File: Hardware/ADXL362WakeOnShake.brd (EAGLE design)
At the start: 43.2 x 24.1 mm, 23 parts, among them J1 PROG_HDR, U1 ADXL362, U3 ADP160-3.3

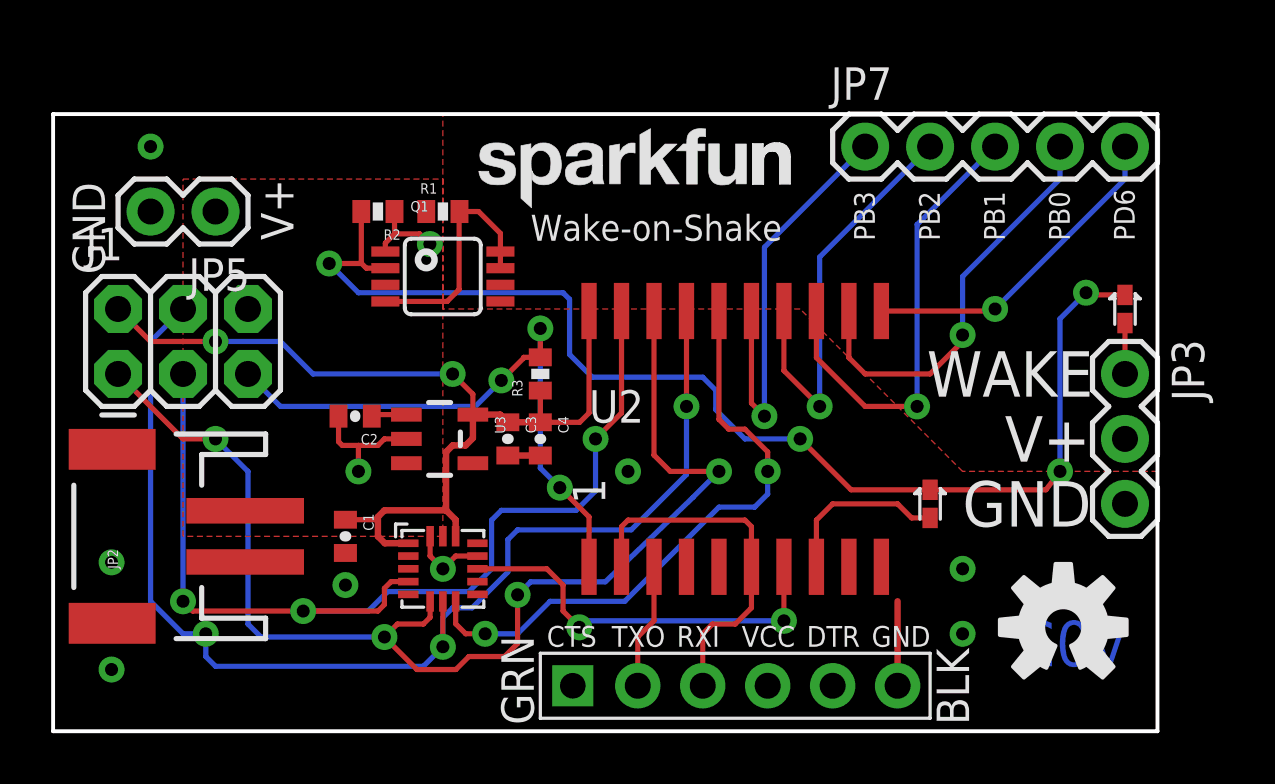
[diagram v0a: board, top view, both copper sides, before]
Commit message: Updating hardware files to v10: - FTDI header silk changed to accurately reflect pin names - moved some traces to avoid silk/via collision - added 10k resistor pull-up on RX line - FTDI header was slightly off grid - added silk on ATTiny package.
Changes to Firmware are purely machine changes to project files.
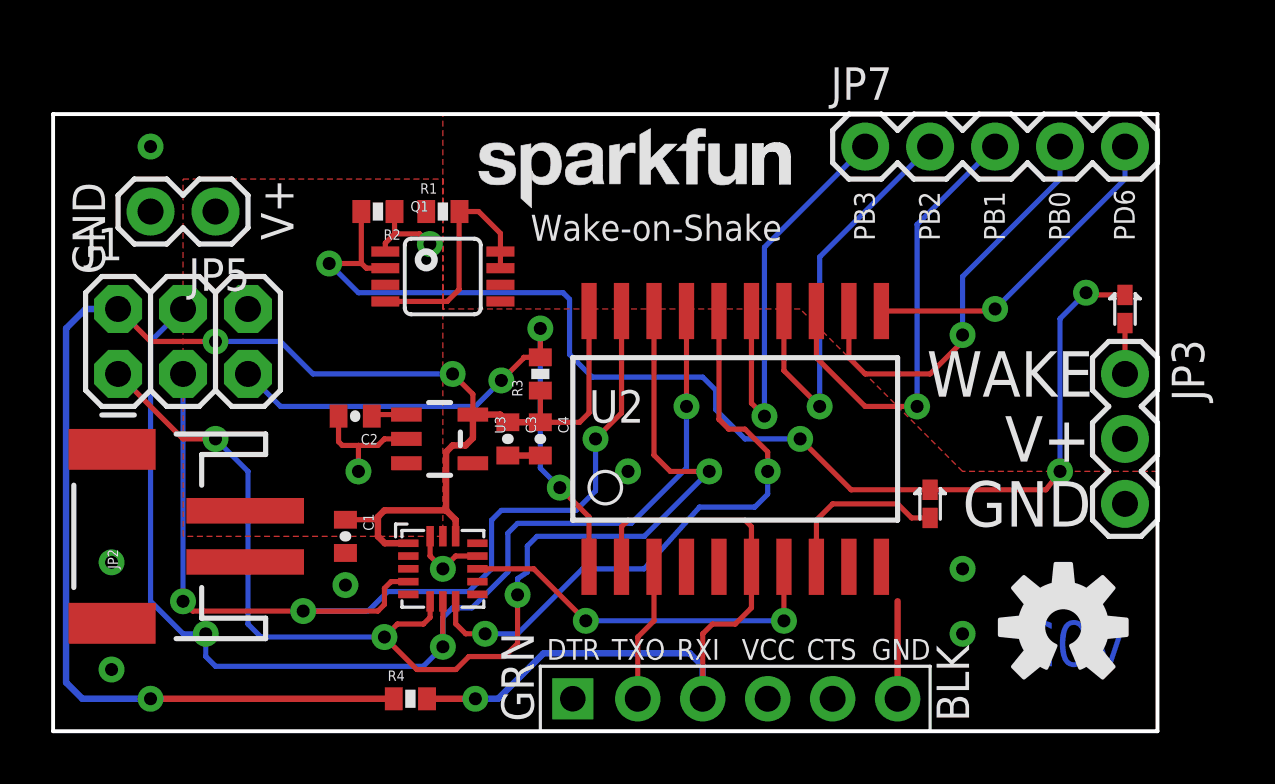
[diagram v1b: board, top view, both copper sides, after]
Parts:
- added R4: 10k, SparkFun-Passives:0402-RES
- moved JP1 0.51 mm to (26.7, 1.27)
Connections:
- net 3.3V: now also R4.1
- net RXI: now also R4.2
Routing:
- net 3.3V: track 38.2 -> 67.5 mm, vias 2 -> 3
- net RXI: track 15.1 -> 28.6 mm, vias 0 -> 1
- net INT1: track 15.7 -> 14.9 mm
- net TXO: track 4.92 -> 5.42 mm
- net GND: track 16.4 -> 16.9 mm
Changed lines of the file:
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@@
 </element>
 <element name="JP3" library="SparkFun-Connectors" package="1X03" value="" x="41.91" y="13.97" rot="R270"/>
-<element name="JP1" library="SparkFun-Connectors" package="FTDI_DEVICE_SIDE" value="FTDI_DEVICE" x="26.67" y="1.778"/>
+<element name="JP1" library="SparkFun-Connectors" package="FTDI_DEVICE_SIDE" value="FTDI_DEVICE" x="26.67" y="1.27"/>
 <element name="D2" library="SparkFun-DiscreteSemi" package="SOD-523" value="RB751" x="34.29" y="8.89" rot="R90">
 <attribute name="PROD_ID" value="DIO-11018" x="34.29" y="8.89" size="1.778" layer="27" font="vector" ratio="15" rot="R90" display="off"/>
@@
 <attribute name="DIST_ID" value="ADP160AUJZ-3.3-R7TR-ND" x="15.113" y="11.43" size="1.778" layer="27" rot="R270" display="off"/>
 <attribute name="DIST" value="Digikey" x="15.113" y="11.43" size="1.778" layer="27" rot="R270" display="off"/>
+<attribute name="PROD_ID" value="VREG-11306" x="15.113" y="11.43" size="1.778" layer="27" rot="R270" display="off"/>
+<attribute name="VALUE" value="ADP160" x="15.113" y="11.43" size="1.778" layer="27" rot="R270" display="off"/>
 </element>
 <element name="R2" library="SparkFun-Passives" package="0402-RES" value="1M" x="12.7" y="20.32" rot="R180">
@@
 <element name="JP6" library="SparkFun-Aesthetics" package="SFE-NEW-WEBLOGO" value="LOGO-SFENEW" x="36.322" y="15.494" rot="MR0"/>
 <element name="JP7" library="SparkFun-Connectors" package="1X05" value="" x="31.75" y="22.86"/>
+<element name="R4" library="SparkFun-Passives" package="0402-RES" value="10k" x="13.97" y="1.27">
+<attribute name="PROD_ID" value="RES-00824" x="13.97" y="1.27" size="1.778" layer="27" font="vector" ratio="15" display="off"/>
+</element>
 </elements>
 <signals>
@@
 <contactref element="JP1" pad="P$6"/>
 <wire x1="32.385" y1="6.43" x2="32.385" y2="5.715" width="0.254" layer="1"/>
-<wire x1="33.02" y1="5.08" x2="33.02" y2="1.778" width="0.254" layer="1"/>
+<wire x1="33.02" y1="5.08" x2="33.02" y2="1.27" width="0.254" layer="1"/>
 <wire x1="17.78" y1="10.78" x2="19.05" y2="10.78" width="0.254" layer="1"/>
 <wire x1="12.99" y1="18.755" x2="12.99" y2="19.086" width="0.2032" layer="1"/>
@@
 <via x="28.575" y="4.318" extent="1-16" drill="0.508"/>
 <wire x1="28.575" y1="4.318" x2="20.828" y2="4.318" width="0.2032" layer="16"/>
-<wire x1="20.828" y1="4.318" x2="20.574" y2="4.064" width="0.2032" layer="16"/>
-<via x="20.574" y="4.064" extent="1-16" drill="0.508"/>
-<wire x1="20.574" y1="4.064" x2="19.939" y2="4.699" width="0.2032" layer="1"/>
-<wire x1="19.939" y1="4.699" x2="19.939" y2="5.715" width="0.2032" layer="1"/>
-<wire x1="19.939" y1="5.715" x2="19.304" y2="6.35" width="0.2032" layer="1"/>
-<wire x1="19.304" y1="6.35" x2="16.59" y2="6.35" width="0.2032" layer="1"/>
+<via x="20.828" y="4.318" extent="1-16" drill="0.508"/>
+<wire x1="20.828" y1="4.318" x2="18.796" y2="6.35" width="0.2032" layer="1"/>
+<wire x1="18.796" y1="6.35" x2="16.59" y2="6.35" width="0.2032" layer="1"/>
 </signal>
 <signal name="3.3V">
@@
 <wire x1="6.35" y1="15.24" x2="3.81" y2="15.24" width="0.2032" layer="1"/>
 <wire x1="3.81" y1="15.24" x2="2.54" y2="16.51" width="0.2032" layer="1"/>
+<contactref element="R4" pad="1"/>
+<wire x1="13.32" y1="1.27" x2="3.81" y2="1.27" width="0.254" layer="1"/>
+<via x="3.81" y="1.27" extent="1-16" drill="0.508"/>
+<wire x1="3.81" y1="1.27" x2="1.143" y2="1.27" width="0.254" layer="16"/>
+<wire x1="1.143" y1="1.27" x2="0.508" y2="1.905" width="0.254" layer="16"/>
+<wire x1="0.508" y1="1.905" x2="0.508" y2="15.748" width="0.254" layer="16"/>
+<wire x1="0.508" y1="15.748" x2="1.27" y2="16.51" width="0.254" layer="16"/>
+<wire x1="1.27" y1="16.51" x2="2.54" y2="16.51" width="0.254" layer="16"/>
 </signal>
 <signal name="SCK">
@@
 <via x="15.24" y="3.302" extent="1-16" drill="0.508"/>
 <wire x1="16.383" y1="4.826" x2="17.78" y2="6.223" width="0.2032" layer="16"/>
-<wire x1="17.78" y1="6.223" x2="17.78" y2="7.493" width="0.2032" layer="16"/>
-<wire x1="17.78" y1="7.493" x2="18.161" y2="7.874" width="0.2032" layer="16"/>
-<wire x1="18.161" y1="7.874" x2="22.606" y2="7.874" width="0.2032" layer="16"/>
-<wire x1="22.606" y1="7.874" x2="24.765" y2="10.033" width="0.2032" layer="16"/>
-<wire x1="24.765" y1="10.033" x2="24.765" y2="12.7" width="0.2032" layer="16"/>
+<wire x1="17.78" y1="6.223" x2="17.78" y2="7.747" width="0.2032" layer="16"/>
+<wire x1="17.78" y1="7.747" x2="18.161" y2="8.128" width="0.2032" layer="16"/>
+<wire x1="18.161" y1="8.128" x2="22.606" y2="8.128" width="0.2032" layer="16"/>
+<wire x1="22.606" y1="8.128" x2="24.765" y2="10.287" width="0.2032" layer="16"/>
+<wire x1="24.765" y1="10.287" x2="24.765" y2="12.7" width="0.2032" layer="16"/>
 <via x="24.765" y="12.7" extent="1-16" drill="0.508"/>
 <wire x1="24.765" y1="12.7" x2="24.765" y2="16.43" width="0.2032" layer="1"/>
@@
 <wire x1="18.161" y1="3.429" x2="18.161" y2="5.334" width="0.2032" layer="1"/>
 <via x="18.161" y="5.334" extent="1-16" drill="0.508"/>
-<wire x1="18.161" y1="5.334" x2="18.669" y2="5.842" width="0.2032" layer="16"/>
-<wire x1="18.669" y1="5.842" x2="21.59" y2="5.842" width="0.2032" layer="16"/>
-<wire x1="21.59" y1="5.842" x2="25.019" y2="9.144" width="0.2032" layer="16"/>
-<wire x1="25.019" y1="9.144" x2="26.035" y2="10.16" width="0.2032" layer="16"/>
-<via x="26.035" y="10.16" extent="1-16" drill="0.508"/>
-<wire x1="26.035" y1="10.16" x2="24.13" y2="10.16" width="0.2032" layer="1"/>
+<wire x1="18.161" y1="5.334" x2="18.161" y2="5.969" width="0.2032" layer="16"/>
+<wire x1="18.161" y1="5.969" x2="18.542" y2="6.223" width="0.2032" layer="16"/>
+<wire x1="18.542" y1="6.223" x2="18.542" y2="7.239" width="0.2032" layer="16"/>
+<wire x1="18.542" y1="7.239" x2="18.923" y2="7.62" width="0.2032" layer="16"/>
+<wire x1="18.923" y1="7.62" x2="23.114" y2="7.62" width="0.2032" layer="16"/>
+<wire x1="23.114" y1="7.62" x2="25.654" y2="10.16" width="0.2032" layer="16"/>
+<via x="25.654" y="10.16" extent="1-16" drill="0.508"/>
+<wire x1="25.654" y1="10.16" x2="24.13" y2="10.16" width="0.2032" layer="1"/>
 <wire x1="24.13" y1="10.16" x2="23.495" y2="10.795" width="0.2032" layer="1"/>
 <wire x1="23.495" y1="10.795" x2="23.495" y2="16.43" width="0.2032" layer="1"/>
@@
 <via x="16.891" y="3.81" extent="1-16" drill="0.508"/>
 <wire x1="16.891" y1="3.81" x2="18.161" y2="3.81" width="0.2032" layer="16"/>
-<wire x1="18.161" y1="3.81" x2="19.431" y2="5.08" width="0.2032" layer="16"/>
-<wire x1="19.431" y1="5.08" x2="22.352" y2="5.08" width="0.2032" layer="16"/>
-<wire x1="22.352" y1="5.08" x2="26.035" y2="8.763" width="0.2032" layer="16"/>
+<wire x1="18.161" y1="3.81" x2="20.701" y2="6.35" width="0.2032" layer="16"/>
+<wire x1="20.701" y1="6.35" x2="23.114" y2="6.35" width="0.2032" layer="16"/>
+<wire x1="23.114" y1="6.35" x2="25.273" y2="8.763" width="0.2032" layer="16"/>
 <via x="27.94" y="10.16" extent="1-16" drill="0.508"/>
 <wire x1="26.035" y1="16.43" x2="26.035" y2="12.192" width="0.2032" layer="1"/>
@@
 <wire x1="27.051" y1="11.811" x2="27.94" y2="10.922" width="0.2032" layer="1"/>
 <wire x1="27.94" y1="10.922" x2="27.94" y2="10.16" width="0.2032" layer="1"/>
-<wire x1="26.035" y1="8.763" x2="27.432" y2="8.763" width="0.2032" layer="16"/>
+<wire x1="25.273" y1="8.763" x2="27.432" y2="8.763" width="0.2032" layer="16"/>
 <wire x1="27.432" y1="8.763" x2="27.94" y2="9.271" width="0.2032" layer="16"/>
 <wire x1="27.94" y1="9.271" x2="27.94" y2="10.16" width="0.2032" layer="16"/>
@@
 <contactref element="JP1" pad="P$3"/>
 <wire x1="27.305" y1="6.43" x2="27.305" y2="5.715" width="0.254" layer="1"/>
-<wire x1="25.4" y1="1.778" x2="25.4" y2="3.81" width="0.2032" layer="1"/>
+<wire x1="25.4" y1="1.27" x2="25.4" y2="3.81" width="0.2032" layer="1"/>
 <wire x1="25.4" y1="3.81" x2="25.781" y2="4.191" width="0.2032" layer="1"/>
 <wire x1="25.781" y1="4.191" x2="26.67" y2="4.191" width="0.2032" layer="1"/>
@@
 <wire x1="27.051" y1="8.255" x2="27.305" y2="8.001" width="0.2032" layer="1"/>
 <wire x1="27.305" y1="8.001" x2="27.305" y2="6.43" width="0.2032" layer="1"/>
+<contactref element="R4" pad="2"/>
+<wire x1="14.62" y1="1.27" x2="16.51" y2="1.27" width="0.254" layer="1"/>
+<via x="16.51" y="1.27" extent="1-16" drill="0.508"/>
+<wire x1="16.51" y1="1.27" x2="17.399" y2="1.27" width="0.254" layer="16"/>
+<wire x1="17.399" y1="1.27" x2="19.177" y2="3.048" width="0.254" layer="16"/>
+<wire x1="19.177" y1="3.048" x2="24.892" y2="3.048" width="0.254" layer="16"/>
+<wire x1="24.892" y1="3.048" x2="25.4" y2="2.54" width="0.254" layer="16"/>
+<wire x1="25.4" y1="2.54" x2="25.4" y2="1.27" width="0.254" layer="16"/>
 </signal>
 <signal name="TXO">
 <contactref element="U2" pad="3"/>
 <contactref element="JP1" pad="P$2"/>
-<wire x1="22.86" y1="1.778" x2="22.86" y2="3.683" width="0.2032" layer="1"/>
+<wire x1="22.86" y1="1.27" x2="22.86" y2="3.683" width="0.2032" layer="1"/>
 <wire x1="22.86" y1="3.683" x2="23.495" y2="4.318" width="0.2032" layer="1"/>
 <wire x1="23.495" y1="4.318" x2="23.495" y2="6.43" width="0.2032" layer="1"/>
@@
 </signal>
 </signals>
+<errors>
+</errors>
 </board>
 </drawing>
